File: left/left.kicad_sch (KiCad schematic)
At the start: 47 parts, among them J1 USB_C_Receptacle_USB2.0, J2 Conn_01x04, J3 Conn_01x06, SW1 SW_Push, SW10 SW_Push, SW11 SW_Push, SW12 SW_Push, SW13 SW_Push, SW14 SW_Push, SW15 SW_Push, SW16 SW_Push, SW17 SW_Push, SW18 SW_Push, SW19 SW_Push, SW2 SW_Push, SW20 SW_Push, SW21 SW_Push, SW22 SW_Push, SW23 SW_Push, SW24 SW_Push, SW25 SW_Push, SW26 SW_Push, SW27 SW_Push, SW28 SW_Push, SW29 SW_Push, SW3 RotaryEncoder_Switch, SW30 SW_Push, SW31 SW_Push, SW32 SW_Push, SW33 SW_Push, SW34 SW_Push, SW4 SW_Push, SW5 SW_Push, SW6 SW_Push, SW7 SW_Push, SW8 SW_Push, SW9 SW_Push, U1 HOLYIOT-18010-NRF52840

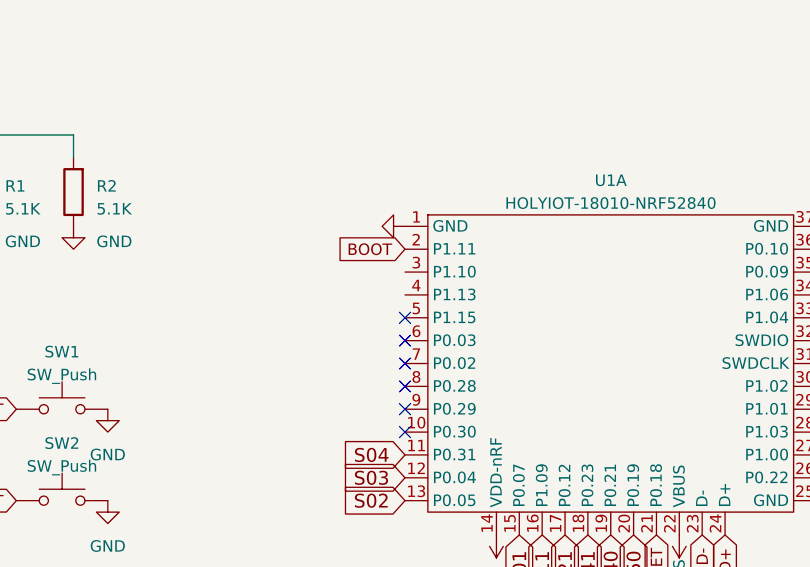
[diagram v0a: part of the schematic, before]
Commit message: update footprint of rf module
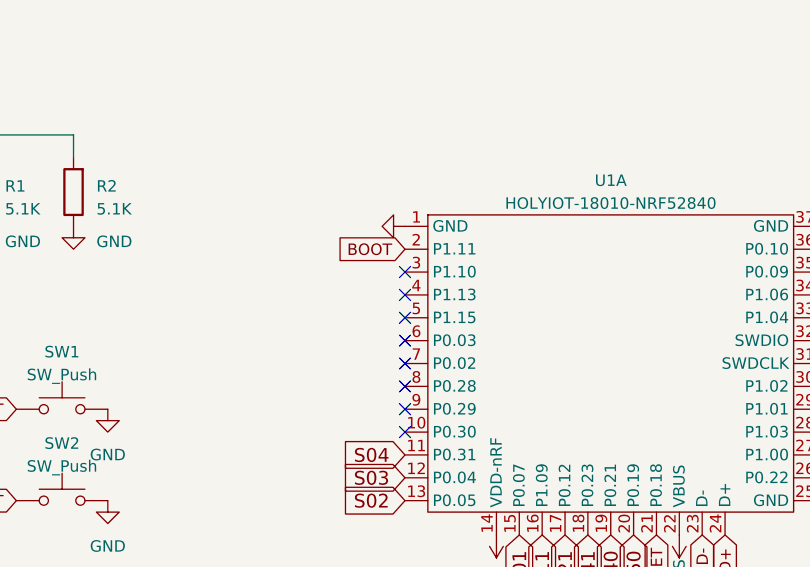
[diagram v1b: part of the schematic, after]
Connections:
- no-connect marks 9 -> 11
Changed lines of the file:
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@@
   (no_connect (at 40.64 46.99))
   (no_connect (at 40.64 49.53))
+  (no_connect (at 104.14 39.37))
+  (no_connect (at 104.14 41.91))
   (no_connect (at 104.14 44.45))
   (no_connect (at 104.14 46.99))
@@
       (effects (font (size 1.524 1.524)) hide)
     )
-    (property "Datasheet" "" (id 3) (at 63.5 168.91 0)
+    (property "Datasheet" "~" (id 3) (at 63.5 168.91 0)
       (effects (font (size 1.524 1.524)))
     )
@@
       (effects (font (size 1.524 1.524)) hide)
     )
-    (property "Datasheet" "" (id 3) (at 63.5 179.07 0)
+    (property "Datasheet" "~" (id 3) (at 63.5 179.07 0)
       (effects (font (size 1.524 1.524)))
     )
@@
       (effects (font (size 1.524 1.524)) hide)
     )
-    (property "Datasheet" "" (id 3) (at 63.5 189.23 0)
+    (property "Datasheet" "~" (id 3) (at 63.5 189.23 0)
       (effects (font (size 1.524 1.524)))
     )
@@
       (effects (font (size 1.524 1.524)) hide)
     )
-    (property "Datasheet" "" (id 3) (at 63.5 199.39 0)
+    (property "Datasheet" "~" (id 3) (at 63.5 199.39 0)
       (effects (font (size 1.524 1.524)))
     )
@@
       (effects (font (size 1.524 1.524)) hide)
     )
-    (property "Datasheet" "" (id 3) (at 63.5 209.55 0)
+    (property "Datasheet" "~" (id 3) (at 63.5 209.55 0)
       (effects (font (size 1.524 1.524)))
     )
@@
       (effects (font (size 1.524 1.524)) hide)
     )
-    (property "Datasheet" "" (id 3) (at 86.36 158.75 0)
+    (property "Datasheet" "~" (id 3) (at 86.36 158.75 0)
       (effects (font (size 1.524 1.524)))
     )
@@
       (effects (font (size 1.524 1.524)) hide)
     )
-    (property "Datasheet" "" (id 3) (at 86.36 168.91 0)
+    (property "Datasheet" "~" (id 3) (at 86.36 168.91 0)
       (effects (font (size 1.524 1.524)))
     )
@@
       (effects (font (size 1.524 1.524)) hide)
     )
-    (property "Datasheet" "" (id 3) (at 86.36 179.07 0)
+    (property "Datasheet" "~" (id 3) (at 86.36 179.07 0)
       (effects (font (size 1.524 1.524)))
     )
@@
       (effects (font (size 1.524 1.524)) hide)
     )
-    (property "Datasheet" "" (id 3) (at 86.36 189.23 0)
+    (property "Datasheet" "~" (id 3) (at 86.36 189.23 0)
       (effects (font (size 1.524 1.524)))
     )
@@
       (effects (font (size 1.524 1.524)) hide)
     )
-    (property "Datasheet" "" (id 3) (at 86.36 199.39 0)
+    (property "Datasheet" "~" (id 3) (at 86.36 199.39 0)
       (effects (font (size 1.524 1.524)))
     )
@@
       (effects (font (size 1.524 1.524)) hide)
     )
-    (property "Datasheet" "" (id 3) (at 109.22 158.75 0)
+    (property "Datasheet" "~" (id 3) (at 109.22 158.75 0)
       (effects (font (size 1.524 1.524)))
     )
@@
       (effects (font (size 1.524 1.524)) hide)
     )
-    (property "Datasheet" "" (id 3) (at 109.22 168.91 0)
+    (property "Datasheet" "~" (id 3) (at 109.22 168.91 0)
       (effects (font (size 1.524 1.524)))
     )
@@
       (effects (font (size 1.524 1.524)) hide)
     )
-    (property "Datasheet" "" (id 3) (at 109.22 179.07 0)
+    (property "Datasheet" "~" (id 3) (at 109.22 179.07 0)
       (effects (font (size 1.524 1.524)))
     )
@@
       (effects (font (size 1.524 1.524)) hide)
     )
-    (property "Datasheet" "" (id 3) (at 109.22 189.23 0)
+    (property "Datasheet" "~" (id 3) (at 109.22 189.23 0)
       (effects (font (size 1.524 1.524)))
     )
@@
       (effects (font (size 1.524 1.524)) hide)
     )
-    (property "Datasheet" "" (id 3) (at 109.22 199.39 0)
+    (property "Datasheet" "~" (id 3) (at 109.22 199.39 0)
       (effects (font (size 1.524 1.524)))
     )
@@
       (effects (font (size 1.524 1.524)) hide)
     )
-    (property "Datasheet" "" (id 3) (at 132.08 158.75 0)
+    (property "Datasheet" "~" (id 3) (at 132.08 158.75 0)
       (effects (font (size 1.524 1.524)))
     )
@@
       (effects (font (size 1.524 1.524)) hide)
     )
-    (property "Datasheet" "" (id 3) (at 132.08 168.91 0)
+    (property "Datasheet" "~" (id 3) (at 132.08 168.91 0)
       (effects (font (size 1.524 1.524)))
     )
@@
       (effects (font (size 1.524 1.524)) hide)
     )
-    (property "Datasheet" "" (id 3) (at 132.08 179.07 0)
+    (property "Datasheet" "~" (id 3) (at 132.08 179.07 0)
       (effects (font (size 1.524 1.524)))
     )
@@
       (effects (font (size 1.524 1.524)) hide)
     )
-    (property "Datasheet" "" (id 3) (at 132.08 189.23 0)
+    (property "Datasheet" "~" (id 3) (at 132.08 189.23 0)
       (effects (font (size 1.524 1.524)))
     )
@@
       (effects (font (size 1.524 1.524)) hide)
     )
-    (property "Datasheet" "" (id 3) (at 132.08 199.39 0)
+    (property "Datasheet" "~" (id 3) (at 132.08 199.39 0)
       (effects (font (size 1.524 1.524)))
     )
@@
       (effects (font (size 1.524 1.524)) hide)
     )
-    (property "Datasheet" "" (id 3) (at 154.94 158.75 0)
+    (property "Datasheet" "~" (id 3) (at 154.94 158.75 0)
       (effects (font (size 1.524 1.524)))
     )
@@
       (effects (font (size 1.524 1.524)) hide)
     )
-    (property "Datasheet" "" (id 3) (at 154.94 168.91 0)
+    (property "Datasheet" "~" (id 3) (at 154.94 168.91 0)
       (effects (font (size 1.524 1.524)))
     )
@@
       (effects (font (size 1.524 1.524)) hide)
     )
-    (property "Datasheet" "" (id 3) (at 154.94 179.07 0)
+    (property "Datasheet" "~" (id 3) (at 154.94 179.07 0)
       (effects (font (size 1.524 1.524)))
     )
@@
       (effects (font (size 1.524 1.524)) hide)
     )
-    (property "Datasheet" "" (id 3) (at 154.94 189.23 0)
+    (property "Datasheet" "~" (id 3) (at 154.94 189.23 0)
       (effects (font (size 1.524 1.524)))
     )
@@
       (effects (font (size 1.524 1.524)) hide)
     )
-    (property "Datasheet" "" (id 3) (at 154.94 199.39 0)
+    (property "Datasheet" "~" (id 3) (at 154.94 199.39 0)
       (effects (font (size 1.524 1.524)))
     )
@@
       (effects (font (size 1.524 1.524)) hide)
     )
-    (property "Datasheet" "" (id 3) (at 177.8 158.75 0)
+    (property "Datasheet" "~" (id 3) (at 177.8 158.75 0)
       (effects (font (size 1.524 1.524)))
     )
@@
       (effects (font (size 1.524 1.524)) hide)
     )
-    (property "Datasheet" "" (id 3) (at 177.8 168.91 0)
+    (property "Datasheet" "~" (id 3) (at 177.8 168.91 0)
       (effects (font (size 1.524 1.524)))
     )
@@
       (effects (font (size 1.524 1.524)) hide)
     )
-    (property "Datasheet" "" (id 3) (at 177.8 179.07 0)
+    (property "Datasheet" "~" (id 3) (at 177.8 179.07 0)
       (effects (font (size 1.524 1.524)))
     )
@@
       (effects (font (size 1.524 1.524)) hide)
     )
-    (property "Datasheet" "" (id 3) (at 177.8 189.23 0)
+    (property "Datasheet" "~" (id 3) (at 177.8 189.23 0)
       (effects (font (size 1.524 1.524)))
     )
@@
       (effects (font (size 1.524 1.524)) hide)
     )
-    (property "Datasheet" "" (id 3) (at 177.8 199.39 0)
+    (property "Datasheet" "~" (id 3) (at 177.8 199.39 0)
       (effects (font (size 1.524 1.524)))
     )
@@
     (pin "S2")
   )
-  (symbol (lib_name "blackwing:HOLYIOT-18010-NRF52840_1") (lib_id "blackwing:HOLYIOT-18010-NRF52840") (at 124.46 86.36 0) (unit 2)
+  (symbol (lib_id "blackwing:HOLYIOT-18010-NRF52840") (at 124.46 86.36 0) (unit 2)
     (in_bom yes) (on_board yes)
     (property "Reference" "U1" (id 0) (at 124.46 85.09 0))
@@
     (pin "S1")
   )
-  (symbol (lib_name "blackwing:HOLYIOT-18010-NRF52840_2") (lib_id "blackwing:HOLYIOT-18010-NRF52840") (at 127 30.48 0) (unit 1)
+  (symbol (lib_id "blackwing:HOLYIOT-18010-NRF52840") (at 127 30.48 0) (unit 1)
     (in_bom yes) (on_board yes)
     (property "Reference" "U1" (id 0) (at 127 29.21 0))
